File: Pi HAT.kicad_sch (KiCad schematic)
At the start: 11 parts, among them J4 Barrel_Jack, J7 GPIO_CONNECTOR, Q1 S8550

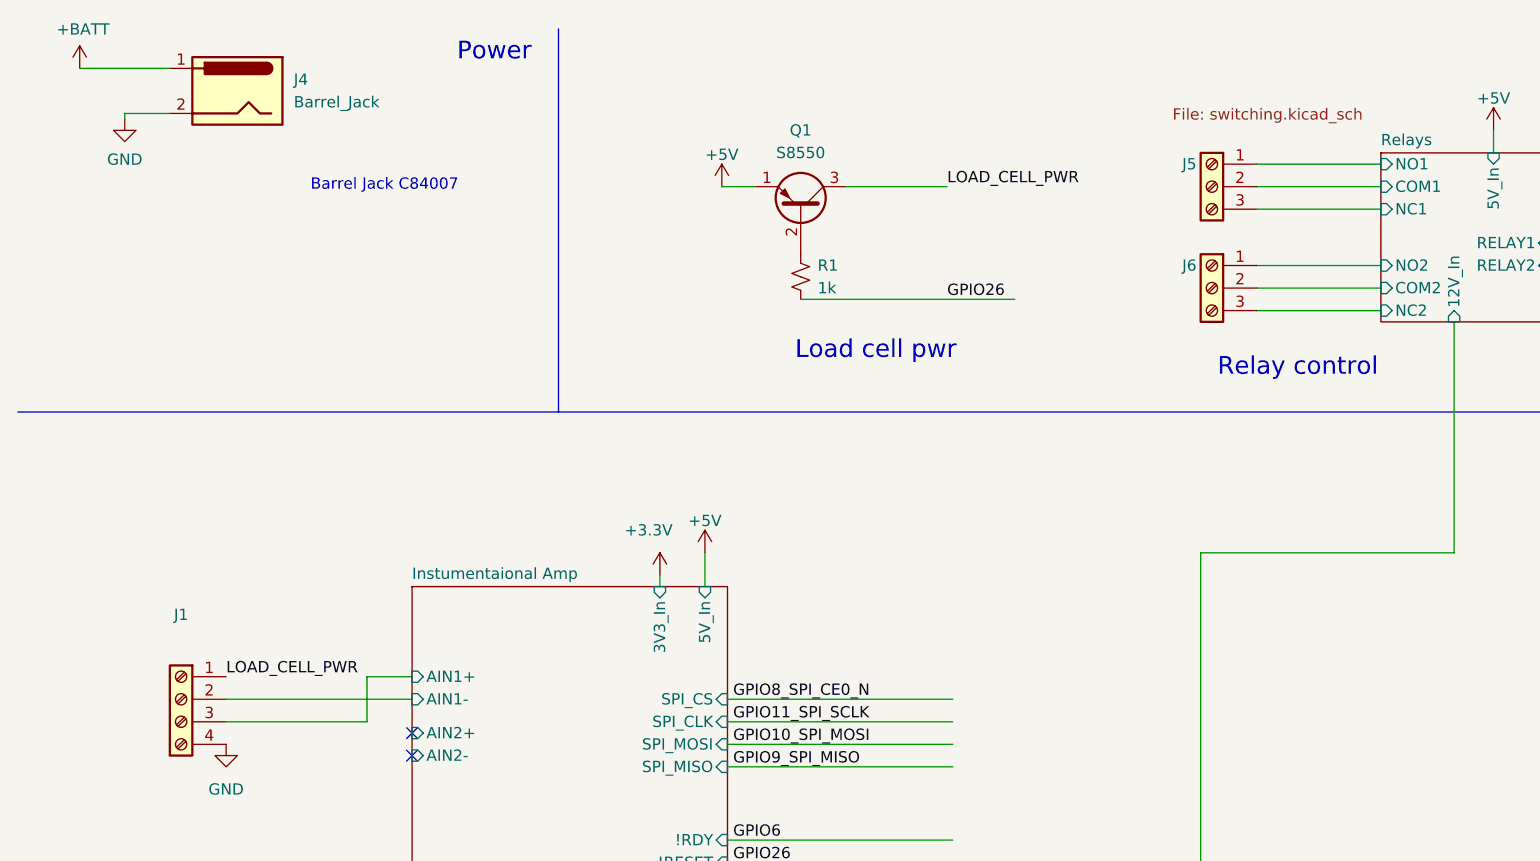
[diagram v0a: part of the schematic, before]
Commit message: Fixed CE pins. Added GND copper pour on F.Cu.
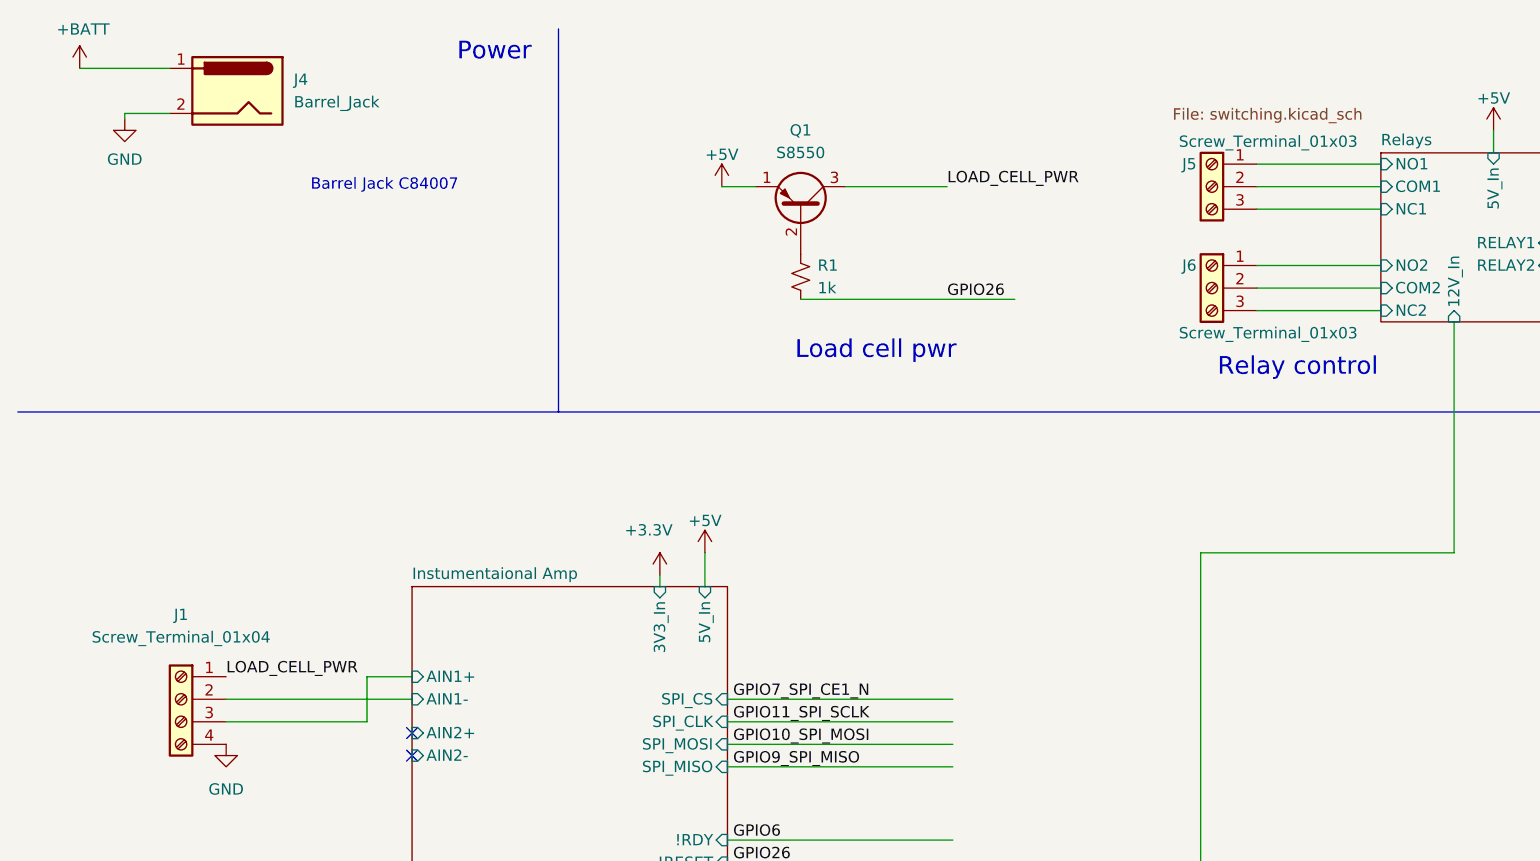
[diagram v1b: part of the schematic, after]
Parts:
- J1: value (none) -> Screw_Terminal_01x04; footprint (none) -> TerminalBlock_Phoenix:TerminalBlock_Phoenix_PT-1,5-4-3.5-H_1x04_P3.50mm_Horizontal
- J5, J6: value (none) -> Screw_Terminal_01x03; footprint (none) -> TerminalBlock_Phoenix:TerminalBlock_Phoenix_PT-1,5-3-3.5-H_1x03_P3.50mm_Horizontal
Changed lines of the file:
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@@
     (effects (font (size 1.27 1.27)) (justify left bottom))
   )
-  (label "GPIO8_SPI_CE0_N" (at 93.345 88.265 0)
+  (label "GPIO7_SPI_CE1_N" (at 93.345 88.265 0)
     (effects (font (size 1.27 1.27)) (justify left bottom))
   )
@@
     (in_bom yes) (on_board yes) (fields_autoplaced)
     (property "Reference" "J1" (id 0) (at 31.115 78.74 0))
-    (property "Value" "" (id 1) (at 31.115 81.28 0))
-    (property "Footprint" "" (id 2) (at 31.115 88.265 0)
+    (property "Value" "Screw_Terminal_01x04" (id 1) (at 31.115 81.28 0))
+    (property "Footprint" "TerminalBlock_Phoenix:TerminalBlock_Phoenix_PT-1,5-4-3.5-H_1x04_P3.50mm_Horizontal" (id 2) (at 31.115 88.265 0)
       (effects (font (size 1.27 1.27)) hide)
     )
@@
     (in_bom yes) (on_board yes)
     (property "Reference" "J5" (id 0) (at 144.78 27.94 0))
-    (property "Value" "" (id 1) (at 153.67 25.4 0))
-    (property "Footprint" "" (id 2) (at 147.32 30.48 0)
+    (property "Value" "Screw_Terminal_01x03" (id 1) (at 153.67 25.4 0))
+    (property "Footprint" "TerminalBlock_Phoenix:TerminalBlock_Phoenix_PT-1,5-3-3.5-H_1x03_P3.50mm_Horizontal" (id 2) (at 147.32 30.48 0)
       (effects (font (size 1.27 1.27)) hide)
     )
@@
     (in_bom yes) (on_board yes)
     (property "Reference" "J6" (id 0) (at 144.78 39.37 0))
-    (property "Value" "" (id 1) (at 153.67 46.99 0))
-    (property "Footprint" "" (id 2) (at 147.32 41.91 0)
-      (effects (font (size 1.27 1.27)) hide)
-    )
+    (property "Value" "Screw_Terminal_01x03" (id 1) (at 153.67 46.99 0))
+    (property "Footprint" "TerminalBlock_Phoenix:TerminalBlock_Phoenix_PT-1,5-3-3.5-H_1x03_P3.50mm_Horizontal" (id 2) (at 147.32 41.91 0)
+      (effects (font (size 1.27 1.27)) hide)
+    )

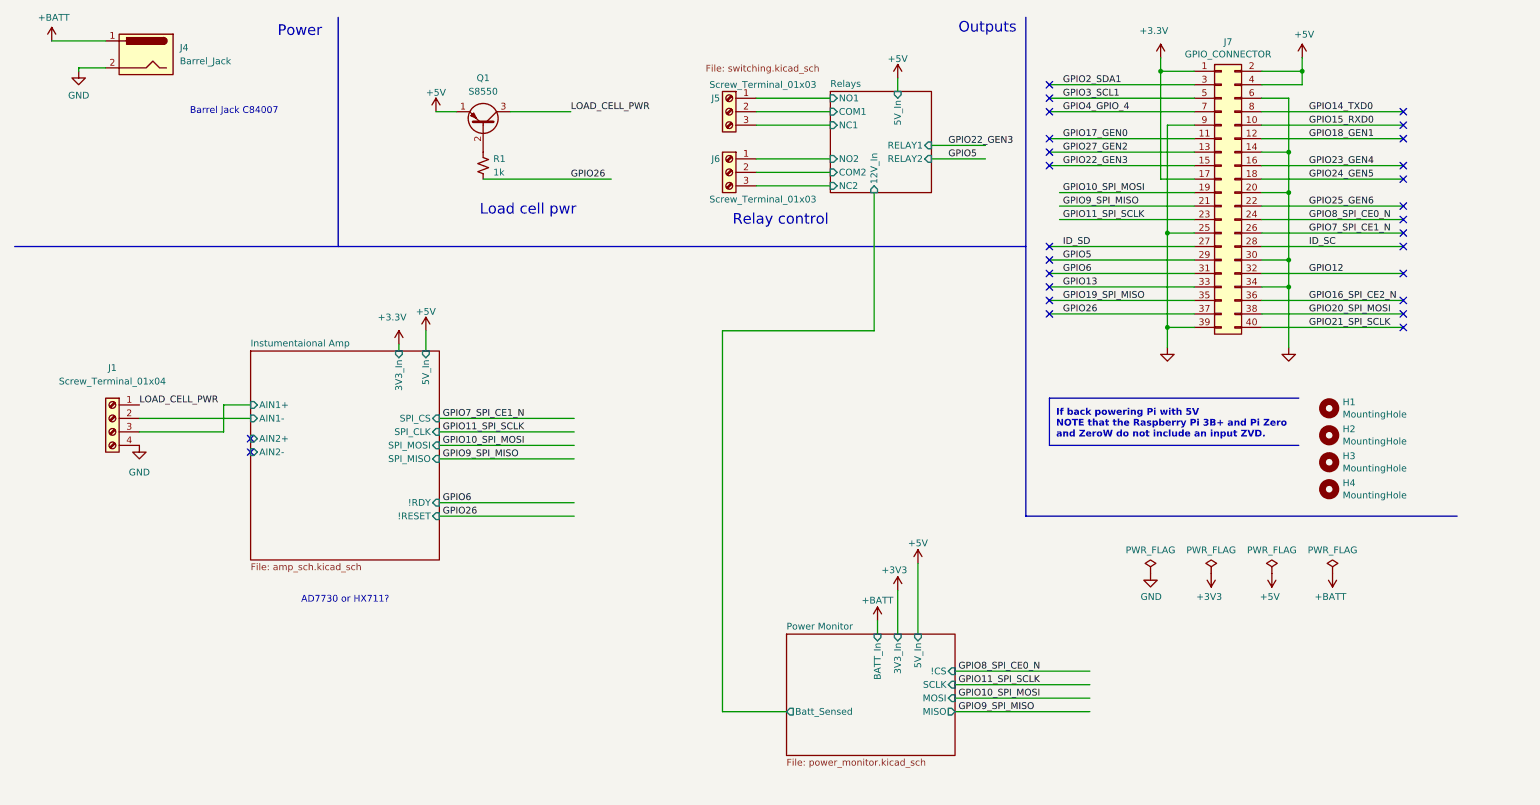
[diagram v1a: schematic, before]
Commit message: Review and fixes on schematic and pcb.
-Updated Relay LED values.
-Fixed !RDY and R1 pin conflict on GPIO26.
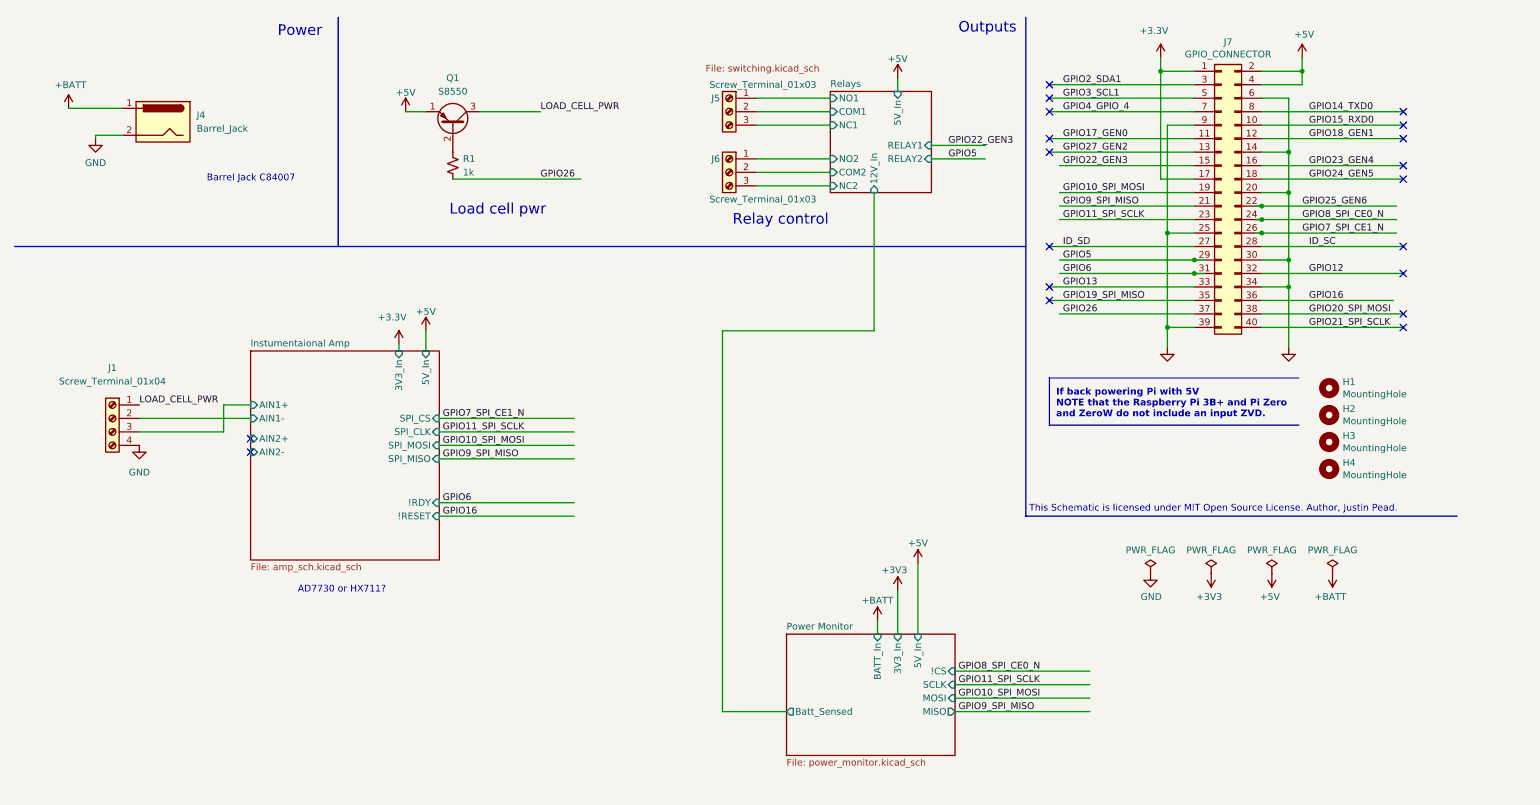
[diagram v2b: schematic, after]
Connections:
- net GPIO16_SPI_CE2_N renamed GPIO16
- no-connect marks 27 -> 19
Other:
- note added: "This Schematic is licensed under MIT Open Source License. Author, Justin Pead."
- title: Raspberry Pi Zero (W) uHAT Template Board -> Raspberry Pi Zero Intrumentation HAT
- moved on the sheet: H1, H2, H3, H4, J4, Q1, R1

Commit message: Improvements made to the info in the schematic excel sheet and made the files necessary for production
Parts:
- H1, H2, H3, H4, J1, J5, J6, J7: Populate (none) -> 0
- J4: Extended (none) -> 1; LCSC (none) -> C84007; Populate (none) -> 1
- Q1: Extended (none) -> 0; LCSC (none) -> C8542; Populate (none) -> 1
- R1: Extended (none) -> 0; LCSC (none) -> C11702; Populate (none) -> 1
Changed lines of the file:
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@@
+      (effects (font (size 1.27 1.27)) hide)
+    )
+    (property "Populate" "0" (id 4) (at 240.03 45.72 0)
       (effects (font (size 1.27 1.27)) hide)
     )
@@
       (effects (font (size 1.27 1.27)) hide)
     )
+    (property "Populate" "0" (id 4) (at 260.35 82.55 0)
+      (effects (font (size 1.27 1.27)) hide)
+    )
   )
   (symbol (lib_id "Mechanical:MountingHole") (at 260.35 87.63 0) (unit 1)
@@
       (effects (font (size 1.27 1.27)) hide)
     )
+    (property "Populate" "0" (id 4) (at 260.35 87.63 0)
+      (effects (font (size 1.27 1.27)) hide)
+    )
   )
   (symbol (lib_id "Mechanical:MountingHole") (at 260.35 92.71 0) (unit 1)
@@
       (effects (font (size 1.27 1.27)) hide)
     )
+    (property "Populate" "0" (id 4) (at 260.35 92.71 0)
+      (effects (font (size 1.27 1.27)) hide)
+    )
   )
   (symbol (lib_id "Mechanical:MountingHole") (at 260.35 97.79 0) (unit 1)
@@
     )
     (property "Datasheet" "~" (id 3) (at 260.35 97.79 0)
+      (effects (font (size 1.27 1.27)) hide)
+    )
+    (property "Populate" "0" (id 4) (at 260.35 97.79 0)
       (effects (font (size 1.27 1.27)) hide)
     )
@@
       (effects (font (size 1.27 1.27)) hide)
     )
+    (property "Populate" "0" (id 4) (at 31.115 88.265 0)
+      (effects (font (size 1.27 1.27)) hide)
+    )
     (pin "1")
     (pin "2")
@@
       (effects (font (size 1.27 1.27)) hide)
     )
+    (property "Populate" "0" (id 4) (at 147.32 30.48 0)
+      (effects (font (size 1.27 1.27)) hide)
+    )
     (pin "1")
     (pin "2")
@@
     )
     (property "Datasheet" "~" (id 3) (at 39.37 33.401 0)
+      (effects (font (size 1.27 1.27)) hide)
+    )
+    (property "LCSC" "C84007" (id 4) (at 40.64 32.385 0)
+      (effects (font (size 1.27 1.27)) hide)
+    )
+    (property "Populate" "1" (id 5) (at 40.64 32.385 0)
+      (effects (font (size 1.27 1.27)) hide)
+    )
+    (property "Extended" "1" (id 6) (at 40.64 32.385 0)
       (effects (font (size 1.27 1.27)) hide)
     )
@@
       (effects (font (size 1.27 1.27)) hide)
     )
+    (property "Populate" "0" (id 4) (at 147.32 41.91 0)
+      (effects (font (size 1.27 1.27)) hide)
+    )
     (pin "1")
     (pin "2")
@@
     )
     (property "Datasheet" "~" (id 3) (at 95.25 40.64 0)
+      (effects (font (size 1.27 1.27)) hide)
+    )
+    (property "Populate" "1" (id 4) (at 95.25 40.64 0)
+      (effects (font (size 1.27 1.27)) hide)
+    )
+    (property "Extended" "0" (id 5) (at 95.25 40.64 0)
+      (effects (font (size 1.27 1.27)) hide)
+    )
+    (property "LCSC" "C11702" (id 6) (at 95.25 40.64 0)
       (effects (font (size 1.27 1.27)) hide)
     )
@@
       (effects (font (size 1.27 1.27)) (justify left) hide)
     )
-    (pin "1")
+    (property "Populate" "1" (id 4) (at 95.25 33.02 0)
+      (effects (font (size 1.27 1.27)) hide)
+    )
+    (property "Extended" "0" (id 5) (at 95.25 33.02 0)
+      (effects (font (size 1.27 1.27)) hide)
+    )
+    (property "LCSC" "C8542" (id 6) (at 95.25 33.02 0)
+      (effects (font (size 1.27 1.27)) hide)
+    )
+    (pin "1")

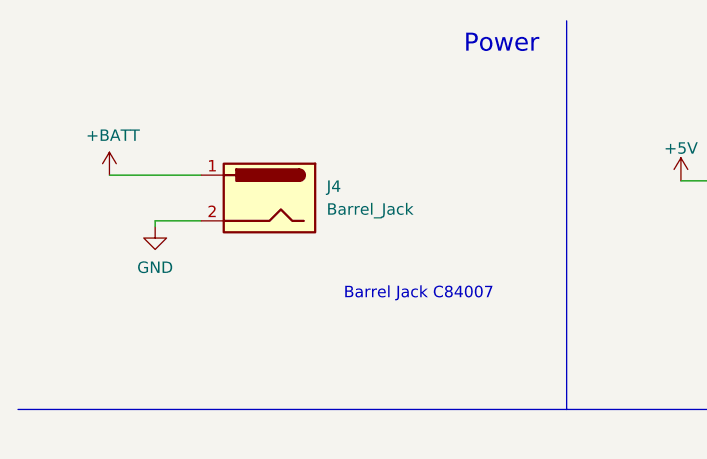
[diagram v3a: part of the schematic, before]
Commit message: Changes to the AD7730 based on Montso's working Arduino system
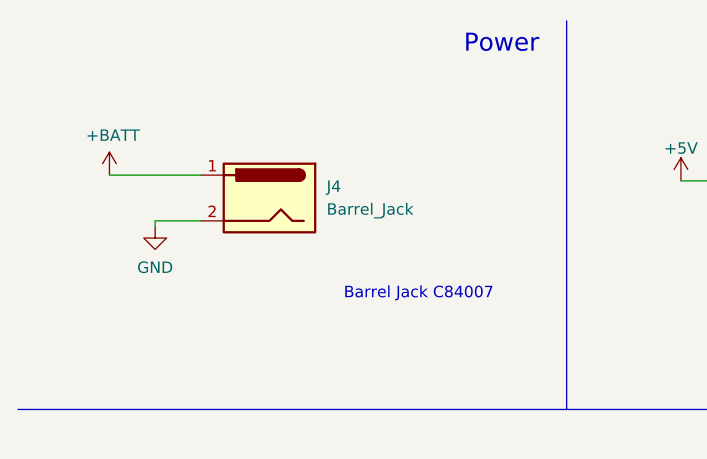
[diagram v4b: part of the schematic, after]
